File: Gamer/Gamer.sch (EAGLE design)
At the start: 53 parts, among them J1 AVR_SPI_PRG_6NS, J2 AVR_SPI_PRG_6NS, J3 AVR_SPI_PRG_6NS, J4 AVR_SPI_PRG_6NS

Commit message: gamer - Starting complete redo of Gamer
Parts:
- removed C10, C11, C8, C9: (no value), resistor:C-USC0603
- removed C6: 0.05uF, resistor:C-USC0603
- removed C7: 1uF, resistor:C-USC0603
- removed J4: AVR_SPI_PRG_6NS, SparkFun-Connectors:AVR_SPI_PRG_6NS
- removed PI-HEADER: (no value), pinhead:PINHD-2X13
- removed R4: Bypass, resistor:R-US_R0603
- removed R5, R6, R8, R9: 100K, resistor:R-US_R0603
- removed R7: 10, resistor:R-US_R0603
- removed U$1, U$13, U$3, U$8: 8X8_LED_MATRIX, ScottSilver:8X8_LED_MATRIX
- removed U$10, U$14, U$4, U$5: ULN2803AFWG, ScottSilver:ULN2803AFWG
- removed U$11, U$15, U$6, U$9: ATTINY48, ScottSilver:ATTINY48
- removed U$12, U$16, U$2, U$7: RES_ARRAY, ScottSilver:RES_ARRAY
- removed U$17, U$18, U$19, U$20, U$21, U$22: 12X12MM_BUTTON, ScottSilver:12X12MM_BUTTON
- removed U$23: MMA8653FCR1, ScottSilver:MMA8653FCR1
- removed U$24, U$26: SMDTACTILE, ScottSilver:SMDTACTILE
- removed U$25: LM386, ScottSilver:LM386
- removed U$29: DF3_1X2, ScottSilver:DF3_1X2
- removed U$30: DF3_1X5, ScottSilver:DF3_1X5
- added A, B, DOWN, LEFT, RIGHT, UP: 12X12MM_BUTTON, Gamer:12X12MM_BUTTON
- added P1: (no value), HeaderConnectorBoard:PINHD-2X20
- added P2: NONE, LED_Matrix:PINHD-1X6
- added PROG: NONE, LED_Matrix:PINHD-2X3
- added SELECT, START: 6X6MM_BUTTON, Gamer:6X6MM_BUTTON
- added U1: MMA8653FCR1, AccelBreakout:MMA8653FCR1
- added U2: ATTINY48, LED_Matrix:ATTINY48
- added U3: ULN2803AFWG, LED_Matrix:ULN2803AFWG
- C1, C2, C3, C4: device resistor:C-USC0603 -> AccelBreakout:C-USC0603
- C5: value (none) -> 1uF; device resistor:CPOL-US153CLV-0605 -> resistor:C-USC0603
- J1: value AVR_SPI_PRG_6NS -> NONE; device SparkFun-Connectors:AVR_SPI_PRG_6NS -> LED_Matrix:PINHD-1X6
- J2, J3: value AVR_SPI_PRG_6NS -> HEADER-1X8; device SparkFun-Connectors:AVR_SPI_PRG_6NS -> LED_Matrix:HEADER-1X8
- R1, R2: value 1k -> 10K; device resistor:R-US_R0603 -> AccelBreakout:R-US_R0603
- R3: value Bypass -> 10k
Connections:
- removed net A: PI-HEADER.7, U$22.3
- removed net AUDIO: U$25.+INPUT, U$30.1
- removed net B: PI-HEADER.11, U$21.3
- removed net DOWN: PI-HEADER.18, U$20.2
- removed net LEFT: PI-HEADER.16, U$18.2
- removed net MISO1/MOSI2: J1.1, J2.4, R3.1, U$6.PB3, U$9.PB4
- removed net MISO2/MOSI3: J2.1, J4.4, R4.1, U$15.PB3, U$6.PB4
- removed net MISO3/MOSI4: J3.4, J4.1, U$11.PB3, U$15.PB4
- removed net N$1: U$1.COL0, U$5.O1
- removed net N$10: U$1.ROW6, U$2.2R
- removed net N$100: U$11.PC4, U$12.R2
- removed net N$101: U$11.PC5, U$12.R1
- removed net N$102: U$15.PC7, U$16.R8
- removed net N$103: U$13.COL0, U$14.O1
- removed net N$104: U$13.COL1, U$14.O2
- removed net N$105: U$13.COL2, U$14.O3
- removed net N$106: U$13.COL3, U$14.O4
- removed net N$107: U$13.COL4, U$14.O5
- removed net N$108: U$13.COL5, U$14.O6
- removed net N$109: U$13.COL6, U$14.O7
- removed net N$11: U$1.ROW5, U$2.3R
- removed net N$110: U$13.COL7, U$14.O8
- removed net N$111: U$13.ROW7, U$16.1R
- removed net N$112: U$13.ROW6, U$16.2R
- removed net N$113: U$13.ROW5, U$16.3R
- removed net N$114: U$13.ROW4, U$16.4R
- removed net N$115: U$13.ROW3, U$16.5R
- removed net N$116: U$13.ROW2, U$16.6R
- removed net N$117: U$13.ROW1, U$16.7R
- removed net N$118: U$13.ROW0, U$16.8R
- removed net N$119: U$14.I1, U$15.PD0
- removed net N$12: U$1.ROW4, U$2.4R
- removed net N$120: U$14.I2, U$15.PD1
- removed net N$121: U$14.I3, U$15.PD2
- removed net N$122: U$14.I4, U$15.PD3
- removed net N$123: U$14.I5, U$15.PD4
- removed net N$124: U$14.I6, U$15.PD5
- removed net N$125: U$14.I7, U$15.PD6
- removed net N$126: U$14.I8, U$15.PD7
- removed net N$129: U$15.PC0, U$16.R6
- removed net N$13: U$1.ROW3, U$2.5R
- removed net N$130: U$15.PC1, U$16.R5
- removed net N$131: U$15.PC2, U$16.R4
- removed net N$132: U$15.PC3, U$16.R3
- removed net N$133: U$15.PC4, U$16.R2
- removed net N$134: U$15.PC5, U$16.R1
- removed net N$14: U$1.ROW2, U$2.6R
- removed net N$15: U$1.ROW1, U$2.7R
- removed net N$16: U$1.ROW0, U$2.8R
- removed net N$17: U$5.I1, U$9.PD0
- removed net N$18: U$5.I2, U$9.PD1
- removed net N$19: U$5.I3, U$9.PD2
- removed net N$2: U$1.COL1, U$5.O2
- removed net N$20: U$5.I4, U$9.PD3
- removed net N$21: U$5.I5, U$9.PD4
- removed net N$22: U$5.I6, U$9.PD5
- removed net N$23: U$5.I7, U$9.PD6
- removed net N$24: U$5.I8, U$9.PD7
- removed net N$25: U$2.R7, U$9.PA1
- removed net N$26: U$2.R8, U$9.PC7
- removed net N$27: U$2.R6, U$9.PC0
- removed net N$28: U$2.R5, U$9.PC1
- removed net N$29: U$2.R4, U$9.PC2
- removed net N$3: U$1.COL2, U$5.O3
- removed net N$30: U$2.R3, U$9.PC3
- removed net N$31: U$2.R2, U$9.PC4
- removed net N$32: U$2.R1, U$9.PC5
- removed net N$33: C7.1, U$25.BYPASS
- removed net N$35: C5.+, C6.1, U$25.VOUT
- removed net N$36: U$3.COL0, U$4.O1
- removed net N$37: C6.2, R7.2
- removed net N$38: U$3.COL1, U$4.O2
- removed net N$39: U$3.COL2, U$4.O3
- removed net N$4: U$1.COL3, U$5.O4
- removed net N$40: U$3.COL3, U$4.O4
- removed net N$41: U$3.COL4, U$4.O5
- removed net N$42: U$3.COL5, U$4.O6
- removed net N$43: U$3.COL6, U$4.O7
- removed net N$44: U$3.COL7, U$4.O8
- removed net N$45: U$3.ROW7, U$7.1R
- removed net N$46: U$3.ROW6, U$7.2R
- removed net N$47: U$3.ROW5, U$7.3R
- removed net N$48: U$3.ROW4, U$7.4R
- removed net N$49: U$3.ROW3, U$7.5R
- removed net N$5: U$1.COL4, U$5.O5
- removed net N$50: U$3.ROW2, U$7.6R
- removed net N$51: U$3.ROW1, U$7.7R
- removed net N$52: U$3.ROW0, U$7.8R
- removed net N$53: U$4.I1, U$6.PD0
- removed net N$54: U$4.I2, U$6.PD1
- removed net N$55: U$4.I3, U$6.PD2
- removed net N$56: U$4.I4, U$6.PD3
- removed net N$57: U$4.I5, U$6.PD4
- removed net N$58: U$4.I6, U$6.PD5
- removed net N$59: U$4.I7, U$6.PD6
- removed net N$6: U$1.COL5, U$5.O6
- removed net N$60: U$4.I8, U$6.PD7
- removed net N$61: U$6.PA1, U$7.R7
- removed net N$62: U$6.PC7, U$7.R8
- removed net N$63: U$6.PC0, U$7.R6
- removed net N$64: U$6.PC1, U$7.R5
- removed net N$65: U$6.PC2, U$7.R4
- removed net N$66: U$6.PC3, U$7.R3
- removed net N$67: U$6.PC4, U$7.R2
- removed net N$68: U$6.PC5, U$7.R1
- removed net N$69: U$15.PA1, U$16.R7
- removed net N$7: U$1.COL6, U$5.O7
- removed net N$70: U$10.O1, U$8.COL0
- removed net N$71: U$10.O2, U$8.COL1
- removed net N$72: U$10.O3, U$8.COL2
- removed net N$73: U$10.O4, U$8.COL3
- removed net N$74: U$10.O5, U$8.COL4
- removed net N$75: U$10.O6, U$8.COL5
- removed net N$76: U$10.O7, U$8.COL6
- removed net N$77: U$10.O8, U$8.COL7
- removed net N$78: U$12.1R, U$8.ROW7
- removed net N$79: U$12.2R, U$8.ROW6
- removed net N$8: U$1.COL7, U$5.O8
- removed net N$80: U$12.3R, U$8.ROW5
- removed net N$81: U$12.4R, U$8.ROW4
- removed net N$82: U$12.5R, U$8.ROW3
- removed net N$83: U$12.6R, U$8.ROW2
- removed net N$84: U$12.7R, U$8.ROW1
- removed net N$85: U$12.8R, U$8.ROW0
- removed net N$86: U$10.I1, U$11.PD0
- removed net N$87: U$10.I2, U$11.PD1
- removed net N$88: U$10.I3, U$11.PD2
- removed net N$89: U$10.I4, U$11.PD3
- removed net N$9: U$1.ROW7, U$2.1R
- removed net N$90: U$10.I5, U$11.PD4
- removed net N$91: U$10.I6, U$11.PD5
- removed net N$92: U$10.I7, U$11.PD6
- removed net N$93: U$10.I8, U$11.PD7
- removed net N$94: U$11.PA1, U$12.R7
- removed net N$95: U$11.PC7, U$12.R8
- removed net N$96: U$11.PC0, U$12.R6
- removed net N$97: U$11.PC1, U$12.R5
- removed net N$98: U$11.PC2, U$12.R4
- removed net N$99: U$11.PC3, U$12.R3
- removed net RIGHT: PI-HEADER.12, U$19.2
- removed net SELECT: PI-HEADER.15, U$26.P$1
- removed net SPK: C5.-, U$29.1
- removed net SS: PI-HEADER.24, U$11.PB2, U$15.PB2, U$6.PB2, U$9.PB2
- removed net START: PI-HEADER.13, U$24.P$1
- removed net UP: PI-HEADER.22, U$17.2
- new net 10/MOSI: P1.19
- new net 11/CLK: P1.23
- new net 12: P1.32
- new net 13: P1.33
- new net 14/TX: P1.8
- new net 15/RX: P1.10
- new net 16: P1.36
- new net 17/RTS: B.3, P1.11
- new net 18: P1.12, RIGHT.2
- new net 19: P1.35
- new net 2/SDA: P1.3
- new net 20: P1.38
- new net 21: P1.40
- new net 22: P1.15, SELECT.2
- new net 23: LEFT.2, P1.16
- new net 24: DOWN.2, P1.18
- new net 25: P1.22, UP.2
- new net 26: P1.37
- new net 27: P1.13, START.2
- new net 3.3V_1: P1.1
- new net 3.3V_2: P1.17
- new net 3/SCL: P1.5
- new net 4: A.3, P1.7
- new net 5: P1.29
- new net 5V_1: P1.4
- new net 5V_2: P1.2
- new net 6: P1.31
- new net 7/CE1: P1.26
- new net 8/CE0: P1.24
- new net 9/MISO: P1.21
- new net COL0: J3.8, U3.O1
- new net COL0_SINK: U2.PD0, U3.I1
- new net COL1: J3.7, U3.O2
- new net COL1_SINK: U2.PD1, U3.I2
- new net COL2: J3.3, U3.O3
- new net COL2_SINK: U2.PD2, U3.I3
- new net COL3: J2.3, U3.O4
- new net COL3_SINK: U2.PD3, U3.I4
- new net COL4: J3.2, U3.O5
- new net COL4_SINK: U2.PD4, U3.I5
- new net COL5: J2.5, U3.O6
- new net COL5_SINK: U2.PD5, U3.I6
- new net COL6: J2.6, U3.O7
- new net COL6_SINK: U2.PD6, U3.I7
- new net COL7: J3.5, U3.O8
- new net COL7_SINK: U2.PD7, U3.I8
- new net CS: J1.4, P2.4, U2.PB2
- new net GND2: P1.25
- new net GND3: P1.20
- new net GND4: P1.14
- new net GND5: P1.6
- new net GND6: P1.39
- new net GND7: P1.34
- new net GND8: P1.30
- new net ID1: P1.27
- new net ID2: P1.28
- new net ROW0: J3.1, U2.PC7
- new net ROW1: J3.6, U2.PA1
- new net ROW2: J2.1, U2.PC0
- new net ROW3: J3.4, U2.PC1
- new net ROW4: J2.8, U2.PC2
- new net ROW5: J2.2, U2.PC3
- new net ROW6: J2.7, U2.PC4
- new net ROW7: J2.4, U2.PC5
- net GND: now also A.1, B.1, C5.2, DOWN.4, LEFT.4, P1.9, P2.6, PROG.2, RIGHT.4, SELECT.4, START.4, U1.AAGND, U1.AGND, U1.GND, U2.AGND, U2.GND, U3.GND, UP.4; no longer C10.2, C11.2, C7.2, C8.2, C9.2, J2.6, J3.6, J4.6, PI-HEADER.6, R7.1, U$10.GND, U$11.AGND, U$11.GND, U$14.GND, U$15.AGND, U$15.GND, U$17.4, U$18.4, U$19.4, U$20.4, U$21.1, U$22.1, U$23.AAGND, U$23.AGND, U$23.GND, U$24.P$4, U$25.-INPUT, U$25.GND, U$26.P$4, U$29.2, U$30.2, U$30.5, U$4.GND, U$5.GND, U$6.AGND, U$6.GND, U$9.AGND, U$9.GND
- net INT1: now also U1.INT1; no longer PI-HEADER.10, U$23.INT1
- net INT2: now also U1.INT2; no longer PI-HEADER.8, U$23.INT2
- net MISO: now also J1.3, PROG.5, U2.PB4; no longer J3.1, PI-HEADER.21, R3.2, R4.2, U$11.PB4
- net MOSI: now also P2.3, PROG.4, U2.PB3; no longer J1.4, PI-HEADER.19, U$9.PB3
- net N$34: now also U1.BYP; no longer U$23.BYP
- net RESET: now also P2.5, PROG.1, R3.2, U2.PC6; no longer J2.5, J3.5, J4.5, R5.1, R6.1, R8.1, R9.1, U$11.PC6, U$15.PC6, U$6.PC6, U$9.PC6
- net SCK: now also J1.2, P2.2, PROG.3, U2.PB5; no longer J1.3, J2.3, J3.3, J4.3, PI-HEADER.23, U$11.PB5, U$15.PB5, U$6.PB5, U$9.PB5
- net SCL: now also R1.1, U1.SCL; no longer PI-HEADER.5, R2.2, U$23.SCL
- net SDA: now also R2.1, U1.SDA; no longer PI-HEADER.3, R1.1, U$23.SDA
- net VCC: now also C5.1, J1.1, P2.1, PROG.6, R2.2, R3.1, U1.VDD, U1.VDDIO, U2.AVCC, U2.VCC, U3.COMMON; no longer C10.1, C11.1, C8.1, C9.1, J1.2, J2.2, J3.2, J4.2, R2.1, R5.2, R6.2, R8.2, R9.2, U$10.COMMON, U$11.AVCC, U$11.VCC, U$14.COMMON, U$15.AVCC, U$15.VCC, U$23.VDD, U$23.VDDIO, U$25.VS, U$30.4, U$4.COMMON, U$5.COMMON, U$6.AVCC, U$6.VCC, U$9.AVCC, U$9.VCC
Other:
- note added: "Accelerometer"
- note added: "LED Matrix Connectors"
- note added: "NOTE: PROG header is used bottom-side, so pinout is flipped from Atmel AVR pinout."
- note added: "RasPi Header"

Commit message: gamer - Work in progress
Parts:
- removed J1, P2: NONE, LED_Matrix:PINHD-1X6
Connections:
- removed net 11/CLK: P1.23
- removed net CS: J1.4, P2.4, U2.PB2
- removed net MISO: J1.3, PROG.5, U2.PB4
- removed net SCK: J1.2, P2.2, PROG.3, U2.PB5
- new net 11/SCLK: P1.23, PROG.3, U2.PB5
- net 8/CE0: now also U2.PB2
- net 9/MISO: now also PROG.5, U2.PB4
- net GND: no longer J1.6, P2.6
- net MOSI: no longer P2.3
- net RESET: no longer J1.5, P2.5
- net VCC: no longer J1.1, P2.1
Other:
- moved on the sheet: C5, PROG, R3, U2

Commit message: gamer - Duplicated matrices (not laid out)
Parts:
- added C6, C7, C8: 1uF, resistor:C-USC0603
- added J1, J4, J5, J6, J7, J8: HEADER-1X8, LED_Matrix:HEADER-1X8
- added PROG1, PROG2, PROG3: NONE, LED_Matrix:PINHD-2X3
- added R4, R5, R6: 10k, resistor:R-US_R0603
- added U4, U6, U8: ATTINY48, LED_Matrix:ATTINY48
- added U5, U7, U9: ULN2803AFWG, LED_Matrix:ULN2803AFWG
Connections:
- net COL0_SINK renamed M1_COL0_SINK
- net COL1_SINK renamed M1_COL1_SINK
- net COL2_SINK renamed M1_COL2_SINK
- net COL3_SINK renamed M1_COL3_SINK
- net COL4_SINK renamed M1_COL4_SINK
- net COL5_SINK renamed M1_COL5_SINK
- net COL6_SINK renamed M1_COL6_SINK
- net COL7_SINK renamed M1_COL7_SINK
- net RESET renamed M1_RESET
- removed net COL0: J3.8, U3.O1
- removed net COL1: J3.7, U3.O2
- removed net COL2: J3.3, U3.O3
- removed net COL3: J2.3, U3.O4
- removed net COL4: J3.2, U3.O5
- removed net COL5: J2.5, U3.O6
- removed net COL6: J2.6, U3.O7
- removed net COL7: J3.5, U3.O8
- removed net MOSI: PROG.4, U2.PB3
- removed net ROW0: J3.1, U2.PC7
- removed net ROW1: J3.6, U2.PA1
- removed net ROW2: J2.1, U2.PC0
- removed net ROW3: J3.4, U2.PC1
- removed net ROW4: J2.8, U2.PC2
- removed net ROW5: J2.2, U2.PC3
- removed net ROW6: J2.7, U2.PC4
- removed net ROW7: J2.4, U2.PC5
- new net M1_COL0: J2.8, U3.O1
- new net M1_COL1: J2.7, U3.O2
- new net M1_COL2: J2.3, U3.O3
- new net M1_COL3: J1.3, U3.O4
- new net M1_COL4: J2.2, U3.O5
- new net M1_COL5: J1.5, U3.O6
- new net M1_COL6: J1.6, U3.O7
- new net M1_COL7: J2.5, U3.O8
- new net M1_ROW0: J2.1, U2.PC7
- new net M1_ROW1: J2.6, U2.PA1
- new net M1_ROW2: J1.1, U2.PC0
- new net M1_ROW3: J2.4, U2.PC1
- new net M1_ROW4: J1.8, U2.PC2
- new net M1_ROW5: J1.2, U2.PC3
- new net M1_ROW6: J1.7, U2.PC4
- new net M1_ROW7: J1.4, U2.PC5
- new net M2_COL0: J4.8, U5.O1
- new net M2_COL0_SINK: U4.PD0, U5.I1
- new net M2_COL1: J4.7, U5.O2
- new net M2_COL1_SINK: U4.PD1, U5.I2
- new net M2_COL2: J4.3, U5.O3
- new net M2_COL2_SINK: U4.PD2, U5.I3
- new net M2_COL3: J3.3, U5.O4
- new net M2_COL3_SINK: U4.PD3, U5.I4
- new net M2_COL4: J4.2, U5.O5
- new net M2_COL4_SINK: U4.PD4, U5.I5
- new net M2_COL5: J3.5, U5.O6
- new net M2_COL5_SINK: U4.PD5, U5.I6
- new net M2_COL6: J3.6, U5.O7
- new net M2_COL6_SINK: U4.PD6, U5.I7
- new net M2_COL7: J4.5, U5.O8
- new net M2_COL7_SINK: U4.PD7, U5.I8
- new net M2_RESET: PROG1.1, R4.2, U4.PC6
- new net M2_ROW0: J4.1, U4.PC7
- new net M2_ROW1: J4.6, U4.PA1
- new net M2_ROW2: J3.1, U4.PC0
- new net M2_ROW3: J4.4, U4.PC1
- new net M2_ROW4: J3.8, U4.PC2
- new net M2_ROW5: J3.2, U4.PC3
- new net M2_ROW6: J3.7, U4.PC4
- new net M2_ROW7: J3.4, U4.PC5
- new net M3_COL0: J6.8, U7.O1
- new net M3_COL0_SINK: U6.PD0, U7.I1
- new net M3_COL1: J6.7, U7.O2
- new net M3_COL1_SINK: U6.PD1, U7.I2
- new net M3_COL2: J6.3, U7.O3
- new net M3_COL2_SINK: U6.PD2, U7.I3
- new net M3_COL3: J5.3, U7.O4
- new net M3_COL3_SINK: U6.PD3, U7.I4
- new net M3_COL4: J6.2, U7.O5
- new net M3_COL4_SINK: U6.PD4, U7.I5
- new net M3_COL5: J5.5, U7.O6
- new net M3_COL5_SINK: U6.PD5, U7.I6
- new net M3_COL6: J5.6, U7.O7
- new net M3_COL6_SINK: U6.PD6, U7.I7
- new net M3_COL7: J6.5, U7.O8
- new net M3_COL7_SINK: U6.PD7, U7.I8
- new net M3_RESET: PROG2.1, R5.2, U6.PC6
- new net M3_ROW0: J6.1, U6.PC7
- new net M3_ROW1: J6.6, U6.PA1
- new net M3_ROW2: J5.1, U6.PC0
- new net M3_ROW3: J6.4, U6.PC1
- new net M3_ROW4: J5.8, U6.PC2
- new net M3_ROW5: J5.2, U6.PC3
- new net M3_ROW6: J5.7, U6.PC4
- new net M3_ROW7: J5.4, U6.PC5
- new net M4_COL0: J8.8, U9.O1
- new net M4_COL0_SINK: U8.PD0, U9.I1
- new net M4_COL1: J8.7, U9.O2
- new net M4_COL1_SINK: U8.PD1, U9.I2
- new net M4_COL2: J8.3, U9.O3
- new net M4_COL2_SINK: U8.PD2, U9.I3
- new net M4_COL3: J7.3, U9.O4
- new net M4_COL3_SINK: U8.PD3, U9.I4
- new net M4_COL4: J8.2, U9.O5
- new net M4_COL4_SINK: U8.PD4, U9.I5
- new net M4_COL5: J7.5, U9.O6
- new net M4_COL5_SINK: U8.PD5, U9.I6
- new net M4_COL6: J7.6, U9.O7
- new net M4_COL6_SINK: U8.PD6, U9.I7
- new net M4_COL7: J8.5, U9.O8
- new net M4_COL7_SINK: U8.PD7, U9.I8
- new net M4_RESET: PROG3.1, R6.2, U8.PC6
- new net M4_ROW0: J8.1, U8.PC7
- new net M4_ROW1: J8.6, U8.PA1
- new net M4_ROW2: J7.1, U8.PC0
- new net M4_ROW3: J8.4, U8.PC1
- new net M4_ROW4: J7.8, U8.PC2
- new net M4_ROW5: J7.2, U8.PC3
- new net M4_ROW6: J7.7, U8.PC4
- new net M4_ROW7: J7.4, U8.PC5
- new net MOSI1/MISO2: PROG.4, PROG1.4, PROG2.4, PROG3.4, U2.PB3, U4.PB3, U6.PB3, U8.PB3
- net 11/SCLK: now also PROG1.3, PROG2.3, PROG3.3, U4.PB5, U6.PB5, U8.PB5
- net 8/CE0: now also U4.PB2, U6.PB2, U8.PB2
- net 9/MISO: now also PROG1.5, PROG2.5, PROG3.5, U4.PB4, U6.PB4, U8.PB4
- net GND: now also C6.2, C7.2, C8.2, PROG1.2, PROG2.2, PROG3.2, U4.AGND, U4.GND, U5.GND, U6.AGND, U6.GND, U7.GND, U8.AGND, U8.GND, U9.GND
- net VCC: now also C6.1, C7.1, C8.1, PROG1.6, PROG2.6, PROG3.6, R4.1, R5.1, R6.1, U4.AVCC, U4.VCC, U5.COMMON, U6.AVCC, U6.VCC, U7.COMMON, U8.AVCC, U8.VCC, U9.COMMON

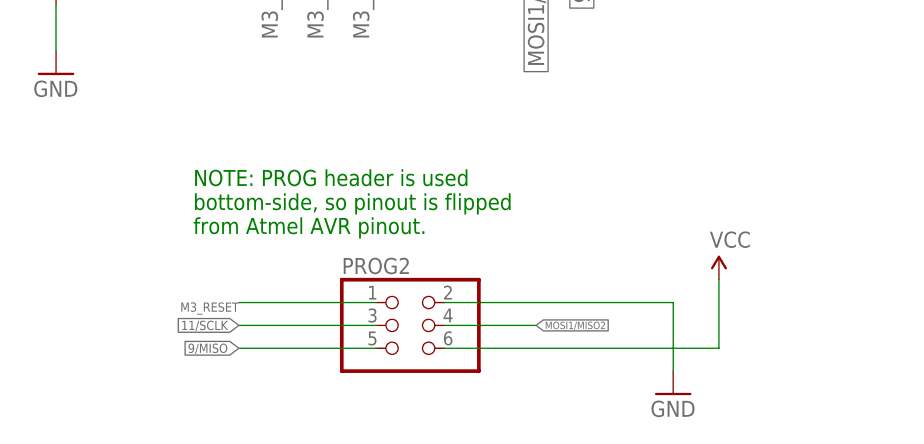
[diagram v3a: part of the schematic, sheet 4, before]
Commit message: gamer - rejiggered PROG connectors
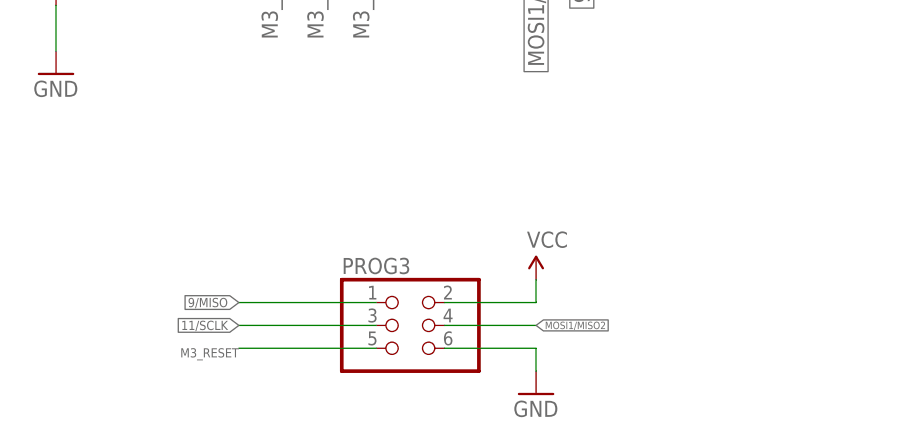
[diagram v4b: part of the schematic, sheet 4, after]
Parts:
- removed PROG: NONE, LED_Matrix:PINHD-2X3
- added PROG4: NONE, Gamer:PINHD-2X3
- PROG1, PROG2, PROG3: device LED_Matrix:PINHD-2X3 -> Gamer:PINHD-2X3
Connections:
- net 11/SCLK: now also PROG4.3; no longer PROG.3
- net 9/MISO: now also PROG1.1, PROG2.1, PROG3.1, PROG4.1; no longer PROG.5, PROG1.5, PROG2.5, PROG3.5
- net GND: now also PROG1.6, PROG2.6, PROG3.6, PROG4.6; no longer PROG.2, PROG1.2, PROG2.2, PROG3.2
- net M1_RESET: now also PROG1.5; no longer PROG.1
- net M2_RESET: now also PROG2.5; no longer PROG1.1
- net M3_RESET: now also PROG3.5; no longer PROG2.1
- net M4_RESET: now also PROG4.5; no longer PROG3.1
- net MOSI1/MISO2: now also PROG4.4; no longer PROG.4
- net VCC: now also PROG1.2, PROG2.2, PROG3.2, PROG4.2; no longer PROG.6, PROG1.6, PROG2.6, PROG3.6
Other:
- note removed: "NOTE: PROG header is used bottom-side, so pinout is flipped from Atmel AVR pinout."

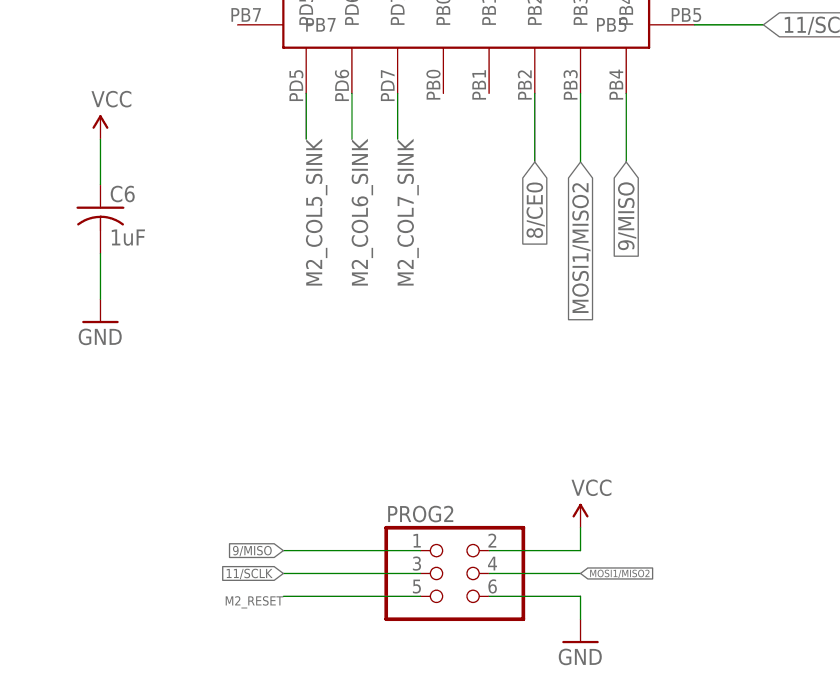
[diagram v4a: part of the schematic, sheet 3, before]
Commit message: gamer - properly chained MISO/MOSI through LED matrices
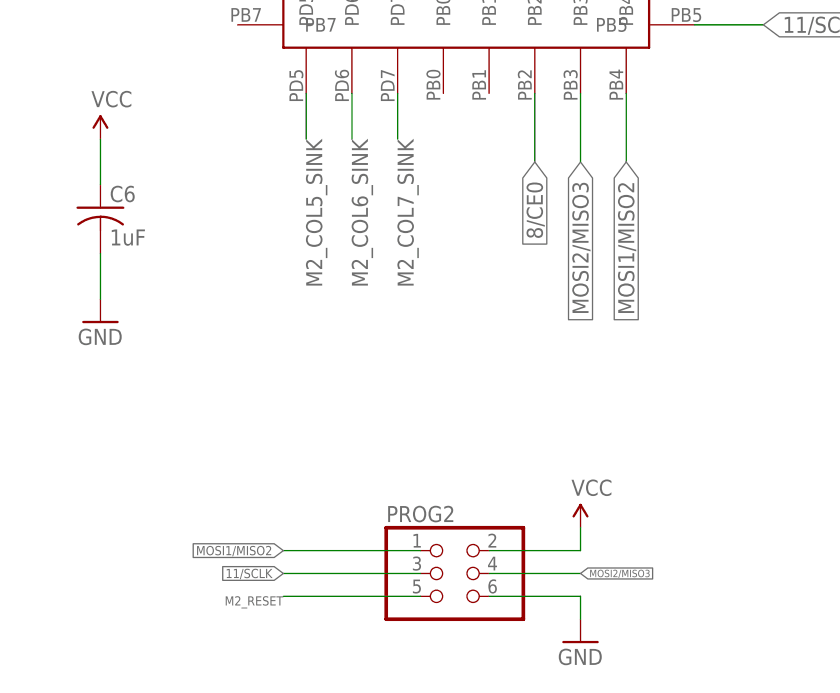
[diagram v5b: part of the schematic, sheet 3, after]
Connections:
- new net 10/MISO: PROG4.4, U8.PB3
- new net MOSI2/MISO3: PROG2.4, PROG3.1, U4.PB3, U6.PB4
- new net MOSI3/MISO4: PROG3.4, PROG4.1, U6.PB3, U8.PB4
- net 9/MISO: no longer PROG2.1, PROG3.1, PROG4.1, U4.PB4, U6.PB4, U8.PB4
- net MOSI1/MISO2: now also PROG2.1, U4.PB4; no longer PROG2.4, PROG3.4, PROG4.4, U4.PB3, U6.PB3, U8.PB3
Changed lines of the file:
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@@
 </segment>
 </net>
-<net name="9/MISO" class="0">
+<net name="MOSI1/MISO2" class="0">
 <segment>
 <pinref part="U4" gate="G$1" pin="PB4"/>
@@
 <pinref part="PROG2" gate="A" pin="1"/>
 <wire x1="50.8" y1="40.64" x2="35.56" y2="40.64" width="0.1524" layer="91"/>
-</segment>
-</net>
-<net name="MOSI1/MISO2" class="0">
-<segment>
-<pinref part="U4" gate="G$1" pin="PB3"/>
-<wire x1="68.58" y1="91.44" x2="68.58" y2="83.82" width="0.1524" layer="91"/>
-<label x="68.58" y="83.82" size="1.778" layer="95" rot="R270" xref="yes"/>
-</segment>
-<segment>
-<label x="68.58" y="38.1" size="0.8128" layer="95" xref="yes"/>
-<pinref part="PROG2" gate="A" pin="4"/>
-<wire x1="58.42" y1="38.1" x2="68.58" y2="38.1" width="0.1524" layer="91"/>
 </segment>
 </net>
@@
 <pinref part="PROG2" gate="A" pin="5"/>
 <wire x1="35.56" y1="35.56" x2="50.8" y2="35.56" width="0.1524" layer="91"/>
+</segment>
+</net>
+<net name="MOSI2/MISO3" class="0">
+<segment>
+<pinref part="U4" gate="G$1" pin="PB3"/>
+<wire x1="68.58" y1="91.44" x2="68.58" y2="83.82" width="0.1524" layer="91"/>
+<label x="68.58" y="83.82" size="1.778" layer="95" rot="R270" xref="yes"/>
+</segment>
+<segment>
+<label x="68.58" y="38.1" size="0.8128" layer="95" xref="yes"/>
+<pinref part="PROG2" gate="A" pin="4"/>
+<wire x1="58.42" y1="38.1" x2="68.58" y2="38.1" width="0.1524" layer="91"/>
 </segment>
 </net>
@@
 </segment>
 </net>
-<net name="9/MISO" class="0">
-<segment>
-<pinref part="U6" gate="G$1" pin="PB4"/>
-<wire x1="73.66" y1="91.44" x2="73.66" y2="83.82" width="0.1524" layer="91"/>
-<label x="73.66" y="83.82" size="1.778" layer="95" rot="R270" xref="yes"/>
-</segment>
-<segment>
-<label x="35.56" y="40.64" size="1.016" layer="95" rot="R180" xref="yes"/>
-<pinref part="PROG3" gate="A" pin="1"/>
-<wire x1="35.56" y1="40.64" x2="50.8" y2="40.64" width="0.1524" layer="91"/>
-</segment>
-</net>
-<net name="MOSI1/MISO2" class="0">
-<segment>
-<pinref part="U6" gate="G$1" pin="PB3"/>
-<wire x1="68.58" y1="91.44" x2="68.58" y2="83.82" width="0.1524" layer="91"/>
-<label x="68.58" y="83.82" size="1.778" layer="95" rot="R270" xref="yes"/>
-</segment>
-<segment>
-<label x="68.58" y="38.1" size="0.8128" layer="95" xref="yes"/>
-<pinref part="PROG3" gate="A" pin="4"/>
-<wire x1="58.42" y1="38.1" x2="68.58" y2="38.1" width="0.1524" layer="91"/>
-</segment>
-</net>
 <net name="M3_COL0_SINK" class="0">
 <segment>
@@
 <pinref part="PROG3" gate="A" pin="5"/>
 <wire x1="35.56" y1="35.56" x2="50.8" y2="35.56" width="0.1524" layer="91"/>
+</segment>
+</net>
+<net name="MOSI2/MISO3" class="0">
+<segment>
+<pinref part="U6" gate="G$1" pin="PB4"/>
+<wire x1="73.66" y1="91.44" x2="73.66" y2="83.82" width="0.1524" layer="91"/>
+<label x="73.66" y="83.82" size="1.778" layer="95" rot="R270" xref="yes"/>
+</segment>
+<segment>
+<label x="35.56" y="40.64" size="1.016" layer="95" rot="R180" xref="yes"/>
+<pinref part="PROG3" gate="A" pin="1"/>
+<wire x1="35.56" y1="40.64" x2="50.8" y2="40.64" width="0.1524" layer="91"/>
+</segment>
+</net>
+<net name="MOSI3/MISO4" class="0">
+<segment>
+<pinref part="U6" gate="G$1" pin="PB3"/>
+<wire x1="68.58" y1="91.44" x2="68.58" y2="83.82" width="0.1524" layer="91"/>
+<label x="68.58" y="83.82" size="1.778" layer="95" rot="R270" xref="yes"/>
+</segment>
+<segment>
+<label x="68.58" y="38.1" size="0.8128" layer="95" xref="yes"/>
+<pinref part="PROG3" gate="A" pin="4"/>
+<wire x1="58.42" y1="38.1" x2="68.58" y2="38.1" width="0.1524" layer="91"/>
 </segment>
 </net>
@@
 </segment>
 </net>
-<net name="9/MISO" class="0">
+<net name="MOSI3/MISO4" class="0">
 <segment>
 <pinref part="U8" gate="G$1" pin="PB4"/>
@@
 </segment>
 </net>
-<net name="MOSI1/MISO2" class="0">
+<net name="10/MISO" class="0">
 <segment>
 <pinref part="U8" gate="G$1" pin="PB3"/>
